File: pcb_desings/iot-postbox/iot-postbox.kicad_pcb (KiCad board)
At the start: 2 copper layers, 23 x 24.7 mm, 16 parts, among them J1 Switch_1, J2 Switch_2, J3 Battery, U1 ESP-12F

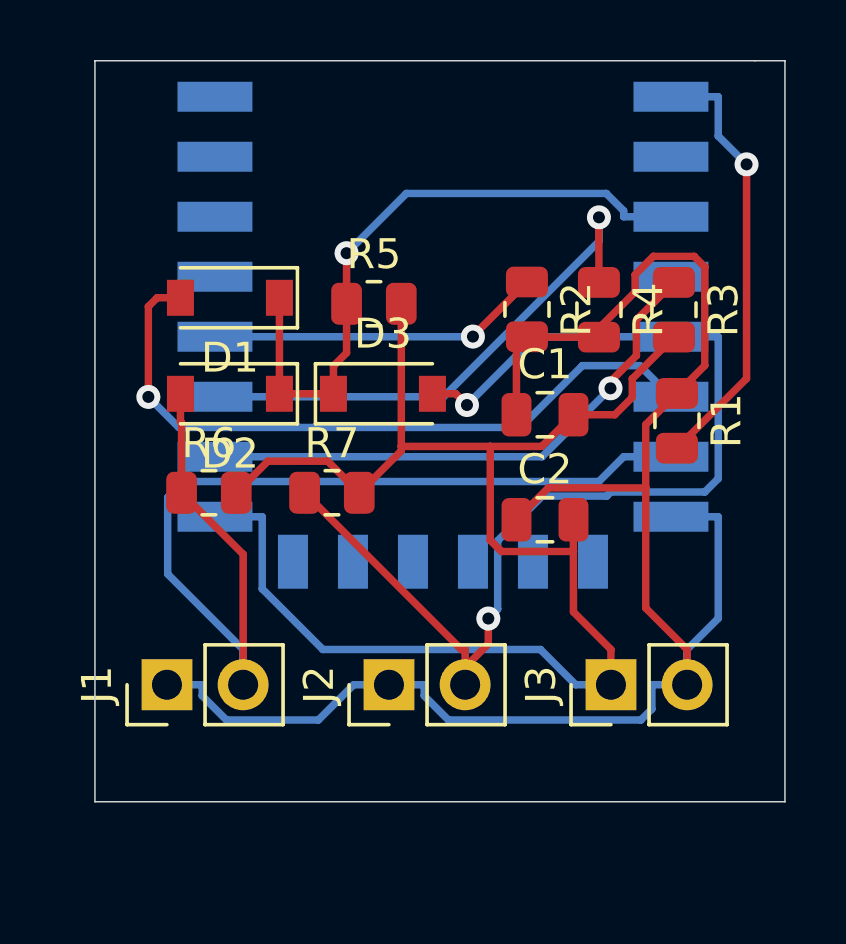
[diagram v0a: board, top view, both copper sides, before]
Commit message: Added uart connection to board sch
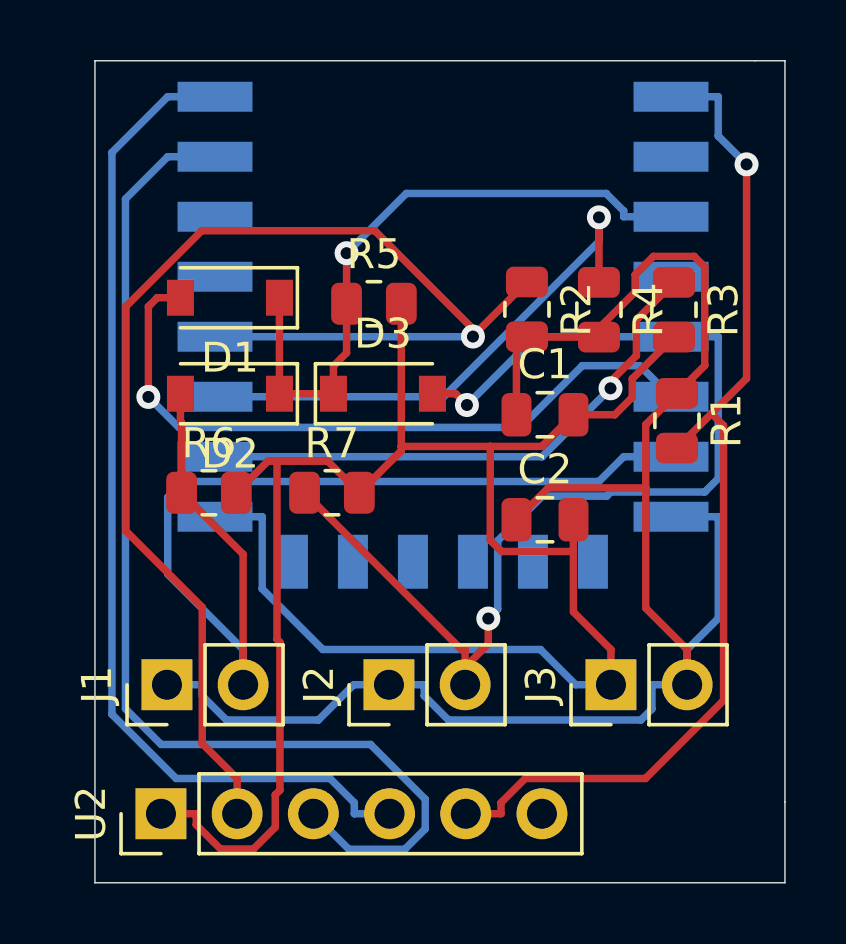
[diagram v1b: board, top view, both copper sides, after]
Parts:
- added U2: TTL_to_USB, Connector_PinHeader_2.54mm:PinHeader_1x06_P2.54mm_Vertical, F.Cu at (164.2, 128.1)
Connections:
- net Net-(R1-Pad2) renamed /RST
- net Net-(R2-Pad1) renamed /GPIO0
- U1 pad 10: Net-(U1-Pad10) -> (no net)
- U1 pad 11: Net-(U1-Pad11) -> (no net)
- U1 pad 12: Net-(U1-Pad12) -> (no net)
- U1 pad 13: Net-(U1-Pad13) -> (no net)
- U1 pad 14: Net-(U1-Pad14) -> (no net)
- U1 pad 19: Net-(U1-Pad19) -> (no net)
- U1 pad 2: Net-(U1-Pad2) -> (no net)
- U1 pad 20: Net-(U1-Pad20) -> (no net)
- U1 pad 21: Net-(U1-Pad21) -> /RX
- U1 pad 22: Net-(U1-Pad22) -> /TX
- U1 pad 4: Net-(U1-Pad4) -> (no net)
- U1 pad 9: Net-(U1-Pad9) -> (no net)
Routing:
- net /RX: track 0.00 -> 37.3 mm
- net /TX: track 0.00 -> 33.8 mm
- net /GPIO0: track 11.2 -> 43.8 mm
- net /RST: track 14.6 -> 34.7 mm
- net GND: track 51.8 -> 68.9 mm
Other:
- board size 23 x 24.7 mm -> 23 x 27.4 mm

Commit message: Updated iot-postbox pcb to v0.0
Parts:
- added C3: 10uF, Capacitor_SMD:C_0805_2012Metric, F.Cu at (112.8, 142.8)
- added C4: 10uF, Capacitor_SMD:C_0805_2012Metric, F.Cu at (112.8, 140.2)
- added C5: 0.1uF, Capacitor_SMD:C_0805_2012Metric, F.Cu at (109.0, 135.5)
- added C6: 1uf, Capacitor_SMD:C_0805_2012Metric, F.Cu at (109.0, 129.1)
- added C7: 1uf, Capacitor_SMD:C_0805_2012Metric, F.Cu at (105.4, 124.7)
- added D4: LED, LED_SMD:LED_0805_2012Metric, F.Cu at (110.6, 151.0)
- added D5: LED, LED_SMD:LED_0805_2012Metric, F.Cu at (106.8, 151.0)
- added J4: USB_B_Micro, Connector_USB:USB_Micro-B_Amphenol_10118194_Horizontal, F.Cu at (118.0, 149.7)
- added J5: Battery, Connector_JST:JST_PH_S2B-PH-SM4-TB_1x02-1MP_P2.00mm_Horizontal, F.Cu at (104.9, 141.3)
- added J6: Battery, Connector_PinHeader_2.54mm:PinHeader_1x02_P2.54mm_Vertical, F.Cu at (102.2, 147.8)
- added R10: 1K, Resistor_SMD:R_0805_2012Metric, F.Cu at (125.4, 140.5)
- added R11: 100, Resistor_SMD:R_0805_2012Metric, F.Cu at (109.0, 132.2)
- added R12: 27K, Resistor_SMD:R_0805_2012Metric, F.Cu at (113.2, 131.2)
- added R13: 100K, Resistor_SMD:R_0805_2012Metric, F.Cu at (113.3, 129.1)
- added R8: 1K, Resistor_SMD:R_0805_2012Metric, F.Cu at (110.4, 147.0)
- added R9: 1K, Resistor_SMD:R_0805_2012Metric, F.Cu at (106.6, 147.0)
- added R_PROG1: 2K, Resistor_SMD:R_0805_2012Metric, F.Cu at (125.4, 145.2)
- added SW1: POWER, MSK12C02:1P2T_SPDT_MSK-C02_7pin, F.Cu at (101.9, 131.7)
- added U3: TP4056, lib:TP4056_SOP-8-PP, F.Cu at (119.0, 142.8)
- added U4: DW01, Package_TO_SOT_SMD:SOT-23-6_Handsoldering, F.Cu at (113.2, 135.1)
- added U5: FS8205A, Package_SO:TSSOP-8_4.4x3mm_P0.65mm, F.Cu at (119.7, 137.0)
- added U6: MCP1700-3302E_SOT23, Package_TO_SOT_SMD:SOT-23, F.Cu at (102.2, 124.7)
- J3: value Battery -> PowerIn
- U1: moved to F.Cu
- U2: value TTL_to_USB -> TTL_UART_adapter_iot_postbox; footprint Connector_PinHeader_2.54mm:PinHeader_1x06_P2.54mm_Vertical -> Connector_PinHeader_2.54mm:PinHeader_1x07_P2.54mm_Vertical
- moved R1 77.5 mm to (104.0, 110.8), turned to 0 degrees
- moved C1 73.1 mm to (104.0, 118.4), turned to 180 degrees
- moved C2 73.1 mm to (104.0, 120.6), turned to 180 degrees
- moved R5 69.6 mm to (101.8, 114.6), turned to 270 degrees
- moved D3 66.5 mm to (105.1, 114.6), turned to 270 degrees
- moved R3 61.1 mm to (125.4, 136.1)
- moved U1 57.1 mm to (116.8, 113.6), turned to 0 degrees
- moved J3 57.0 mm to (128.7, 150.3), turned to 270 degrees
- moved D1 51.2 mm to (118.7, 129.1), turned to 0 degrees
- moved D2 51.2 mm to (118.7, 132.3), turned to 0 degrees
- moved R4 50.7 mm to (128.1, 110.6), turned to 0 degrees
- moved R2 48.3 mm to (128.1, 112.7), turned to 0 degrees
- moved R7 47.6 mm to (123.8, 129.3)
- moved R6 44.5 mm to (123.8, 132.1)
- moved J2 43.1 mm to (129.0, 118.4), turned to 180 degrees
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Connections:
- net GND renamed IN-
- C1 pad 1: +3V3 -> VCC
- C2 pad 1: +3V3 -> VCC
- J1 pad 1: +3V3 -> VCC
- J2 pad 1: +3V3 -> VCC
- J2 pad 2: /GPIO14 -> /GPIO12
- J3 pad 2: +3V3 -> IN+
- R1 pad 1: +3V3 -> VCC
- R2 pad 2: +3V3 -> VCC
- R4 pad 2: +3V3 -> VCC
- R7 pad 1: /GPIO14 -> /GPIO12
- U1 pad 19: (no net) -> /CHRG
- U1 pad 2: (no net) -> /ADC
- U1 pad 20: (no net) -> /STDBY
- U1 pad 8: +3V3 -> VCC
- U2 pad 2: /GPIO0 -> /RX
- U2 pad 3: /RX -> /TX
- U2 pad 4: /TX -> /GPIO0
- U2 pad 6: (no net) -> /CH_PD
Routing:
- net +3V3: track 58.4 -> 0.00 mm
- net VCC: track 0.00 -> 55.6 mm, vias 0 -> 1
- net IN-: track 68.9 -> 123.6 mm, vias 0 -> 4
- net IN+: track 0.00 -> 47.9 mm
- net /STDBY: track 0.00 -> 44.3 mm, vias 0 -> 3
- net /CH_PD: track 21.9 -> 65.5 mm
- net BAT+: track 0.00 -> 41.0 mm
- net /CHRG: track 0.00 -> 40.9 mm, vias 0 -> 3
- net BAT-: track 0.00 -> 36.4 mm, vias 0 -> 3
- net /GPIO14: track 36.9 -> 5.28 mm, vias 2 -> 0
- net /ADC: track 0.00 -> 22.2 mm
- net /GPIO12: track 23.3 -> 42.9 mm, vias 1 -> 2
- net /OUT: track 0.00 -> 16.9 mm
- net Net-(R10-Pad1): track 0.00 -> 16.3 mm
- net /RST: track 34.7 -> 50.2 mm
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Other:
- board size 23 x 27.4 mm -> 31 x 43.6 mm
- net class POWER added: clearance 0.2, trace_width 0.65, via_dia 0.8, via_drill 0.4
- board text added: "BAT+"
- board text added: "BAT-"
- board text added: "Battery Power"
- board text added: "CHPD"
- board text added: "ESP-07 or ESP-12"
- board text added: "ESP8266"
- board text added: "GPIO0"
- board text added: "GPIO12"
- board text added: "GPIO13"
- board text added: "IN+"
- board text added: "IN-"
- board text added: "IoT-PostBox"
- board text added: "Main Power"
- board text added: "OFF/ON"
- board text added: "ON/OFF"
- board text added: "RST"
- board text added: "RX"
- board text added: "Switch_1"
- board text added: "Switch_2"
- board text added: "TTL_UART"
- board text added: "TX"
- board text added: "VCC"
- board text added: "github.com/paclema/iot-postbox"
- board text added: "v.0.0"
